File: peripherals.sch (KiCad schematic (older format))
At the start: 60 parts, among them J1 693022010811, J5 U_FL-R-SMT-1_10_, J6 U_FL-R-SMT-1_10_, J7 DM3AT-SF-PEJM5, U6 NCP163ASN330T1G

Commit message: Started placing main components on PCB. Change of RT battery model and USB flash connector
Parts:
- gave numbers to parts that had none: 21
- renumbered C47 to C100, C48 to C101, C49 to C102, C50 to C103, C51 to C104, C52 to C105, C53 to C106, C54 to C107, C34 to C87, C35 to C88, C36 to C89, C37 to C90, C38 to C91, C39 to C92, C40 to C93, C41 to C94, C42 to C95, C43 to C96, C44 to C97, C45 to C98, C46 to C99, D2 to D16, J1 to J8, L4 to L20, L5 to L21, R38 to R100, R40 to R101, R31 to R91, R32 to R92, R33 to R93, R34 to R94, R36 to R98, R37 to R99, U6 to U10

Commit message: Removed mounting pad for GNSS, changed main antenna model, added wifi ufl connector
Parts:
- removed ANT1: GPS-ANT050-external-antenna, sc606-baseboard-footprints:GPS-ANT050-mounting-pad, symbol sc606-baseboard:GPS-ANT050-external-antenna
- removed ANT2: PRO-OB-572_DCPOL, sc606-baseboard-footprints:PRO-OB-572_2, symbol sc606-baseboard:PRO-OB-572_DCPOL
- removed C102, C103, C89, C91: C_0p5_0402, sc606-baseboard-footprints:0402-cap, symbol sc606-baseboard:C_0p5_0402
- removed C92: C_6p9_0402, sc606-baseboard-footprints:0402-cap, symbol sc606-baseboard:C_6p9_0402
- removed C94: C_0p9_0402, sc606-baseboard-footprints:0402-cap, symbol sc606-baseboard:C_0p9_0402
- removed L20: LQW15AN2N4B00D, sc606-baseboard-footprints:0402-res, symbol sc606-baseboard:LQW15AN2N4B00D
- added C?: C_3p_0402, antmicro-footprints:0402-cap, symbol antmicroCapacitors0402:C_3p_0402
- added C? (x2): C_1u_0402, sc606-baseboard-footprints:0402-cap, symbol sc606-baseboard:C_1u_0402
- added E?: ANT-LTE-CER-T, sc606-baseboard-footprints:XDCR_ANT-LTE-CER-T, symbol sc606-baseboard:ANT-LTE-CER-T
- added J?: U_FL-R-SMT-1_10_, sc606-baseboard-footprints:Coax_Conn_U.FL, symbol sc606-baseboard:U_FL-R-SMT-1_10_
- added L?: HK10056N8S-T, antmicro-footprints:INDC1005X55N, symbol antmicroFixedInductors:HK10056N8S-T
- added R? (x4): R_0R_0402, antmicro-footprints:0402-res, symbol antmicroResistors0402:R_0R_0402
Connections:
- net labels added: ANT-WIFI
- wire segments 151 -> 155
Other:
- note added: "Wi-Fi Antenna\n"
- note removed: "Mounting Pad for GNSS Antenna\n"
- moved on the sheet: C101, C87, C88, C90, C93, C95, C96, C98, C99, J5, J6, L21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

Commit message: Added USB A and C double stack connector
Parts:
- C92: renamed from C?; footprint antmicro-footprints:0402-cap -> sc606-baseboard-footprints:0402-cap; symbol antmicroCapacitors0402:C_3p_0402 -> sc606-baseboard:C_3p_0402
- L20: renamed from L?; footprint antmicro-footprints:INDC1005X55N -> sc606-baseboard-footprints:INDC1005X55N; symbol antmicroFixedInductors:HK10056N8S-T -> sc606-baseboard:HK10056N8S-T
- R126, R127, R128, R129: renamed from R?; footprint antmicro-footprints:0402-res -> sc606-baseboard-footprints:0402-res; symbol antmicroResistors0402:R_0R_0402 -> sc606-baseboard:R_0R_0402
- gave numbers to parts that had none: 4
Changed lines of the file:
@@
 	8100 7750 8100 8050
 $Comp
-L sc606-baseboard:ANT-LTE-CER-T E?
+L sc606-baseboard:ANT-LTE-CER-T E1
 U 1 1 620E9422
 P 3450 7650
-F 0 "E?" H 3534 7679 50  0000 L CNN
+F 0 "E1" H 3534 7679 50  0000 L CNN
 F 1 "ANT-LTE-CER-T" H 3534 7588 50  0000 L CNN
 F 2 "sc606-baseboard-footprints:XDCR_ANT-LTE-CER-T" H 3450 7350 50  0001 L BNN
@@
 $EndComp
 $Comp
-L antmicroCapacitors0402:C_3p_0402 C?
+L sc606-baseboard:C_3p_0402 C92
 U 1 1 6212C05D
 P 2400 7650
-F 0 "C?" V 2142 7650 60  0000 C CNN
+F 0 "C92" V 2142 7650 60  0000 C CNN
 F 1 "C_3p_0402" H 2400 7500 60  0001 C CNN
-F 2 "antmicro-footprints:0402-cap" H 2600 7850 60  0001 L CNN
+F 2 "sc606-baseboard-footprints:0402-cap" H 2600 7850 60  0001 L CNN
 F 3 "" H 2400 7650 50  0001 C CNN
 F 4 "MULTICOMP" H 2600 8050 60  0001 L CNN "Manufacturer"
@@
 	2650 7650 2600 7650
 $Comp
-L sc606-baseboard:GND #PWR?
+L sc606-baseboard:GND #PWR0101
 U 1 1 62165D99
 P 2600 8600
-F 0 "#PWR?" H 2600 8350 50  0001 C CNN
+F 0 "#PWR0101" H 2600 8350 50  0001 C CNN
 F 1 "GND" H 2605 8427 50  0000 C CNN
 F 2 "" H 2600 8600 50  0001 C CNN
@@
 $EndComp
 $Comp
-L sc606-baseboard:GND #PWR?
+L sc606-baseboard:GND #PWR0157
 U 1 1 6216613F
 P 3050 7950
-F 0 "#PWR?" H 3050 7700 50  0001 C CNN
+F 0 "#PWR0157" H 3050 7700 50  0001 C CNN
 F 1 "GND" H 3055 7777 50  0000 C CNN
 F 2 "" H 3050 7950 50  0001 C CNN
@@
 $EndComp
 $Comp
-L sc606-baseboard:GND #PWR?
+L sc606-baseboard:GND #PWR0158
 U 1 1 62166933
 P 2150 7950
-F 0 "#PWR?" H 2150 7700 50  0001 C CNN
+F 0 "#PWR0158" H 2150 7700 50  0001 C CNN
 F 1 "GND" H 2155 7777 50  0000 C CNN
 F 2 "" H 2150 7950 50  0001 C CNN
@@
 $EndComp
 $Comp
-L sc606-baseboard:GND #PWR?
+L sc606-baseboard:GND #PWR0159
 U 1 1 62166E12
 P 3350 7950
-F 0 "#PWR?" H 3350 7700 50  0001 C CNN
+F 0 "#PWR0159" H 3350 7700 50  0001 C CNN
 F 1 "GND" H 3355 7777 50  0000 C CNN
 F 2 "" H 3350 7950 50  0001 C CNN
@@
 	3350 7750 3350 7950
 $Comp
-L antmicroResistors0402:R_0R_0402 R?
+L sc606-baseboard:R_0R_0402 R128
 U 1 1 621B97C1
 P 2800 7650
-F 0 "R?" H 2800 7863 60  0000 C CNN
+F 0 "R128" H 2800 7863 60  0000 C CNN
 F 1 "R_0R_0402" H 2800 7500 60  0001 C CNN
-F 2 "antmicro-footprints:0402-res" H 3000 7850 60  0001 L CNN
+F 2 "sc606-baseboard-footprints:0402-res" H 3000 7850 60  0001 L CNN
 F 3 "" H 2800 7650 50  0001 C CNN
 F 4 "PANASONIC" H 3000 8050 60  0001 L CNN "Manufacturer"
@@
 $EndComp
 $Comp
-L antmicroResistors0402:R_0R_0402 R?
+L sc606-baseboard:R_0R_0402 R127
 U 1 1 621B9CE0
 P 2150 7800
-F 0 "R?" V 2059 7870 60  0000 L CNN
+F 0 "R127" V 2059 7870 60  0000 L CNN
 F 1 "R_0R_0402" H 2150 7650 60  0001 C CNN
-F 2 "antmicro-footprints:0402-res" H 2350 8000 60  0001 L CNN
+F 2 "sc606-baseboard-footprints:0402-res" H 2350 8000 60  0001 L CNN
 F 3 "" H 2150 7800 50  0001 C CNN
 F 4 "PANASONIC" H 2350 8200 60  0001 L CNN "Manufacturer"
@@
 	2950 7650 3050 7650
 $Comp
-L antmicroResistors0402:R_0R_0402 R?
+L sc606-baseboard:R_0R_0402 R129
 U 1 1 621BD57F
 P 3050 7800
-F 0 "R?" V 2959 7870 60  0000 L CNN
+F 0 "R129" V 2959 7870 60  0000 L CNN
 F 1 "R_0R_0402" H 3050 7650 60  0001 C CNN
-F 2 "antmicro-footprints:0402-res" H 3250 8000 60  0001 L CNN
+F 2 "sc606-baseboard-footprints:0402-res" H 3250 8000 60  0001 L CNN
 F 3 "" H 3050 7800 50  0001 C CNN
 F 4 "PANASONIC" H 3250 8200 60  0001 L CNN "Manufacturer"
@@
 	3050 7650 3350 7650
 $Comp
-L antmicroFixedInductors:HK10056N8S-T L?
+L sc606-baseboard:HK10056N8S-T L20
 U 1 1 621F9A28
 P 2600 8300
-F 0 "L?" V 2554 8344 50  0000 L CNN
+F 0 "L20" V 2554 8344 50  0000 L CNN
 F 1 "HK10056N8S-T" V 2645 8344 50  0000 L CNN
-F 2 "antmicro-footprints:INDC1005X55N" H 2600 8200 50  0001 C BNN
+F 2 "sc606-baseboard-footprints:INDC1005X55N" H 2600 8200 50  0001 C BNN
 F 3 "https://www.mouser.pl/datasheet/2/396/mlci04_e-1396612.pdf" H 2600 8300 50  0001 L BNN
 F 4 "Taiyo Yuden" H 2600 8150 50  0001 C CNN "Manufacturer"
@@
 Wi-Fi Antenna\n
 $Comp
-L sc606-baseboard:U_FL-R-SMT-1_10_ J?
+L sc606-baseboard:U_FL-R-SMT-1_10_ J12
 U 1 1 6221D1B4
 P 2900 9600
-F 0 "J?" H 2812 9613 50  0000 R CNN
+F 0 "J12" H 2812 9613 50  0000 R CNN
 F 1 "U_FL-R-SMT-1_10_" H 2812 9522 50  0000 R CNN
 F 2 "sc606-baseboard-footprints:Coax_Conn_U.FL" H 3100 9800 60  0001 L CNN
@@
 ANT-WIFI
 $Comp
-L antmicroResistors0402:R_0R_0402 R?
+L sc606-baseboard:R_0R_0402 R126
 U 1 1 62231121
 P 2100 9600
-F 0 "R?" H 2100 9813 60  0000 C CNN
+F 0 "R126" H 2100 9813 60  0000 C CNN
 F 1 "R_0R_0402" H 2100 9450 60  0001 C CNN
-F 2 "antmicro-footprints:0402-res" H 2300 9800 60  0001 L CNN
+F 2 "sc606-baseboard-footprints:0402-res" H 2300 9800 60  0001 L CNN
 F 3 "" H 2100 9600 50  0001 C CNN
 F 4 "PANASONIC" H 2300 10000 60  0001 L CNN "Manufacturer"
@@
 $EndComp
 $Comp
-L sc606-baseboard:C_1u_0402 C?
+L sc606-baseboard:C_1u_0402 C89
 U 1 1 62233FFC
 P 1850 9950
-F 0 "C?" H 1900 10050 60  0000 L CNN
+F 0 "C89" H 1900 10050 60  0000 L CNN
 F 1 "C_1u_0402" H 1850 9800 60  0001 C CNN
 F 2 "sc606-baseboard-footprints:0402-cap" H 2050 10150 60  0001 L CNN
@@
 $EndComp
 $Comp
-L sc606-baseboard:C_1u_0402 C?
+L sc606-baseboard:C_1u_0402 C91
 U 1 1 62236B43
 P 2350 9950
-F 0 "C?" H 2400 10050 60  0000 L CNN
+F 0 "C91" H 2400 10050 60  0000 L CNN
 F 1 "C_1u_0402" H 2350 9800 60  0001 C CNN
 F 2 "sc606-baseboard-footprints:0402-cap" H 2550 10150 60  0001 L CNN
@@
 $EndComp
 $Comp
-L sc606-baseboard:GND #PWR?
+L sc606-baseboard:GND #PWR0160
 U 1 1 6223716E
 P 1850 10250
-F 0 "#PWR?" H 1850 10000 50  0001 C CNN
+F 0 "#PWR0160" H 1850 10000 50  0001 C CNN
 F 1 "GND" H 1855 10077 50  0000 C CNN
 F 2 "" H 1850 10250 50  0001 C CNN
@@
 $EndComp
 $Comp
-L sc606-baseboard:GND #PWR?
+L sc606-baseboard:GND #PWR0161
 U 1 1 6223764D
 P 2350 10250
-F 0 "#PWR?" H 2350 10000 50  0001 C CNN
+F 0 "#PWR0161" H 2350 10000 50  0001 C CNN
 F 1 "GND" H 2355 10077 50  0000 C CNN
 F 2 "" H 2350 10250 50  0001 C CNN
@@
 $EndComp
 $Comp
-L sc606-baseboard:GND #PWR?
+L sc606-baseboard:GND #PWR0162
 U 1 1 622379B0
 P 2900 9850
-F 0 "#PWR?" H 2900 9600 50  0001 C CNN
+F 0 "#PWR0162" H 2900 9600 50  0001 C CNN
 F 1 "GND" H 2905 9677 50  0000 C CNN
 F 2 "" H 2900 9850 50  0001 C CNN

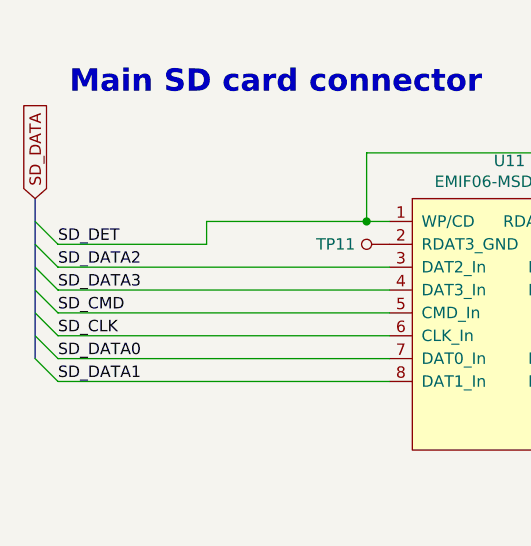
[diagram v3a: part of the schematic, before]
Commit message: Main components placed on board
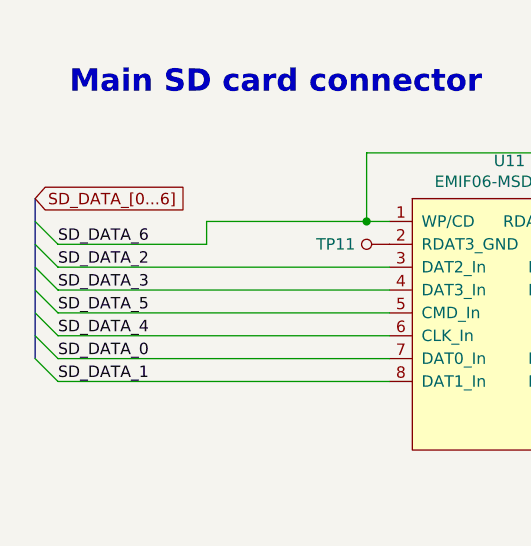
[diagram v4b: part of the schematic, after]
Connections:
- net SD_CLK renamed SD_DATA_4
- net SD_CMD renamed SD_DATA_5
- net SD_DATA0 renamed SD_DATA_0
- net SD_DATA1 renamed SD_DATA_1
- net SD_DATA2 renamed SD_DATA_2
- net SD_DATA3 renamed SD_DATA_3
- net SD_DET renamed SD_DATA_6
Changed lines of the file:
@@
 Main SD card connector
 Text Label 800  1650 0    50   ~ 0
-SD_DET
+SD_DATA_6
 Text Label 800  1850 0    50   ~ 0
-SD_DATA3
+SD_DATA_3
 Text Label 800  1750 0    50   ~ 0
-SD_DATA2
+SD_DATA_2
 Text Label 800  2250 0    50   ~ 0
-SD_DATA1
+SD_DATA_1
 Text Label 800  2150 0    50   ~ 0
-SD_DATA0
+SD_DATA_0
 Text Label 800  1950 0    50   ~ 0
-SD_CMD
+SD_DATA_5
 Text Label 800  2050 0    50   ~ 0
-SD_CLK
+SD_DATA_4
 Wire Wire Line
 	800  1650 1450 1650
@@
 Entry Wire Line
 	700  2150 800  2250
-Text GLabel 700  1450 1    50   Input ~ 0
-SD_DATA
+Text GLabel 700  1450 2    50   Input ~ 0
+SD_DATA_[0...6]
 Text GLabel 3850 1200 1    50   Input ~ 0
 SD_LDO11

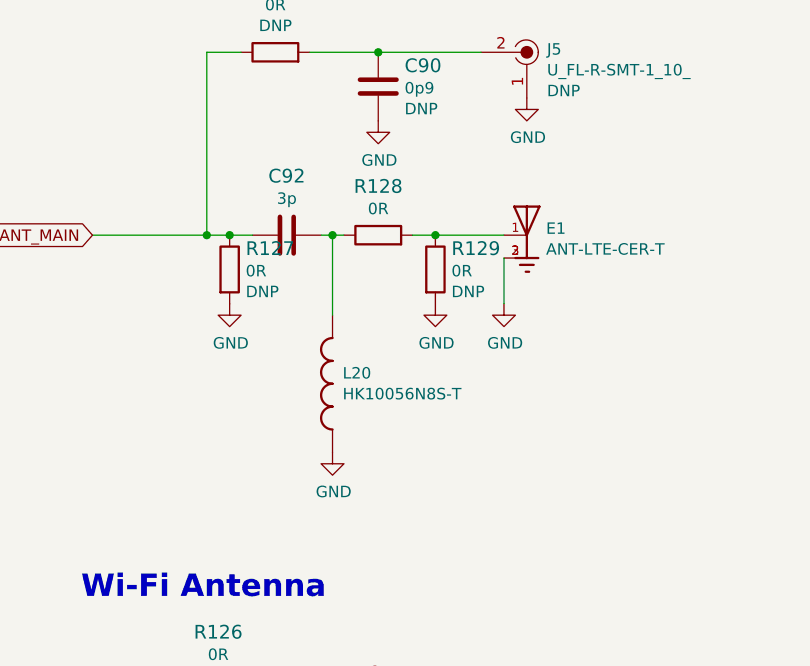
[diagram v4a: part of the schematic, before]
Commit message: FFC and general display camera connectors distributed on board
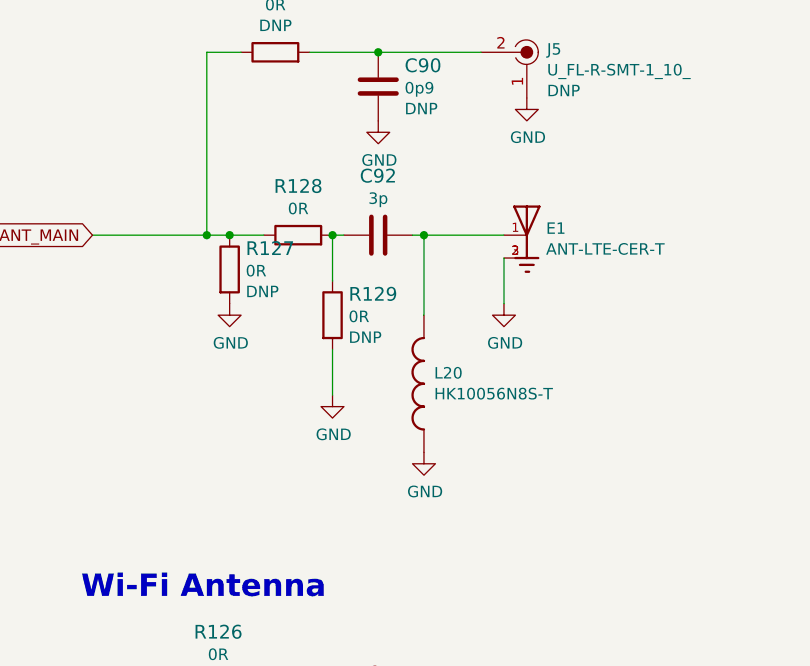
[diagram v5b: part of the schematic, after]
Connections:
- net ANT_MAIN: now also R128.1; no longer C92.2
- net at R128.2, R129.1: now also C92.2; no longer E1.1
- net at C92.1, L20.1: now also E1.1; no longer R128.1
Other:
- moved on the sheet: C92, L20, R128, R129
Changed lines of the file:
@@
 L sc606-baseboard:C_3p_0402 C92
 U 1 1 6212C05D
-P 2400 7650
-F 0 "C92" V 2142 7650 60  0000 C CNN
-F 1 "C_3p_0402" H 2400 7500 60  0001 C CNN
-F 2 "sc606-baseboard-footprints:0402-cap" H 2600 7850 60  0001 L CNN
-F 3 "" H 2400 7650 50  0001 C CNN
-F 4 "MULTICOMP" H 2600 8050 60  0001 L CNN "Manufacturer"
-F 5 "MC0402N3R0C500CT" H 2600 7950 60  0001 L CNN "MPN"
-F 6 "3p" V 2240 7650 50  0000 C CNN "Val"
-	1    2400 7650
-	0    1    1    0
-$EndComp
-Wire Wire Line
-	2250 7650 2150 7650
+P 2800 7650
+F 0 "C92" V 2542 7650 60  0000 C CNN
+F 1 "C_3p_0402" H 2800 7500 60  0001 C CNN
+F 2 "sc606-baseboard-footprints:0402-cap" H 3000 7850 60  0001 L CNN
+F 3 "" H 2800 7650 50  0001 C CNN
+F 4 "MULTICOMP" H 3000 8050 60  0001 L CNN "Manufacturer"
+F 5 "MC0402N3R0C500CT" H 3000 7950 60  0001 L CNN "MPN"
+F 6 "3p" V 2640 7650 50  0000 C CNN "Val"
+	1    2800 7650
+	0    1    1    0
+$EndComp
+Wire Wire Line
+	2300 7650 2150 7650
 Connection ~ 2050 7650
 Wire Wire Line
@@
 L sc606-baseboard:GND #PWR0101
 U 1 1 62165D99
-P 2600 8600
-F 0 "#PWR0101" H 2600 8350 50  0001 C CNN
-F 1 "GND" H 2605 8427 50  0000 C CNN
-F 2 "" H 2600 8600 50  0001 C CNN
-F 3 "" H 2600 8600 50  0001 C CNN
-	1    2600 8600
+P 3000 8600
+F 0 "#PWR0101" H 3000 8350 50  0001 C CNN
+F 1 "GND" H 3005 8427 50  0000 C CNN
+F 2 "" H 3000 8600 50  0001 C CNN
+F 3 "" H 3000 8600 50  0001 C CNN
+	1    3000 8600
 	1    0    0    -1
 $EndComp
@@
 L sc606-baseboard:GND #PWR0157
 U 1 1 6216613F
-P 3050 7950
-F 0 "#PWR0157" H 3050 7700 50  0001 C CNN
-F 1 "GND" H 3055 7777 50  0000 C CNN
-F 2 "" H 3050 7950 50  0001 C CNN
-F 3 "" H 3050 7950 50  0001 C CNN
-	1    3050 7950
+P 2600 8350
+F 0 "#PWR0157" H 2600 8100 50  0001 C CNN
+F 1 "GND" H 2605 8177 50  0000 C CNN
+F 2 "" H 2600 8350 50  0001 C CNN
+F 3 "" H 2600 8350 50  0001 C CNN
+	1    2600 8350
 	1    0    0    -1
 $EndComp
@@
 L sc606-baseboard:R_0R_0402 R128
 U 1 1 621B97C1
-P 2800 7650
-F 0 "R128" H 2800 7863 60  0000 C CNN
-F 1 "R_0R_0402" H 2800 7500 60  0001 C CNN
-F 2 "sc606-baseboard-footprints:0402-res" H 3000 7850 60  0001 L CNN
-F 3 "" H 2800 7650 50  0001 C CNN
-F 4 "PANASONIC" H 3000 8050 60  0001 L CNN "Manufacturer"
-F 5 "ERJ2GE0R00X" H 3000 7950 60  0001 L CNN "MPN"
-F 6 "0R" H 2800 7765 50  0000 C CNN "Val"
-	1    2800 7650
+P 2450 7650
+F 0 "R128" H 2450 7863 60  0000 C CNN
+F 1 "R_0R_0402" H 2450 7500 60  0001 C CNN
+F 2 "sc606-baseboard-footprints:0402-res" H 2650 7850 60  0001 L CNN
+F 3 "" H 2450 7650 50  0001 C CNN
+F 4 "PANASONIC" H 2650 8050 60  0001 L CNN "Manufacturer"
+F 5 "ERJ2GE0R00X" H 2650 7950 60  0001 L CNN "MPN"
+F 6 "0R" H 2450 7765 50  0000 C CNN "Val"
+	1    2450 7650
 	1    0    0    -1
 $EndComp
@@
 Wire Wire Line
 	2150 7650 2050 7650
-Wire Wire Line
-	2950 7650 3050 7650
 $Comp
 L sc606-baseboard:R_0R_0402 R129
 U 1 1 621BD57F
-P 3050 7800
-F 0 "R129" V 2959 7870 60  0000 L CNN
-F 1 "R_0R_0402" H 3050 7650 60  0001 C CNN
-F 2 "sc606-baseboard-footprints:0402-res" H 3250 8000 60  0001 L CNN
-F 3 "" H 3050 7800 50  0001 C CNN
-F 4 "PANASONIC" H 3250 8200 60  0001 L CNN "Manufacturer"
-F 5 "ERJ2GE0R00X" H 3250 8100 60  0001 L CNN "MPN"
-F 6 "0R" V 3057 7870 50  0000 L CNN "Val"
-F 7 "DNP" V 3148 7870 50  0000 L CNN "DNP"
-	1    3050 7800
-	0    1    1    0
-$EndComp
-Connection ~ 3050 7650
-Wire Wire Line
-	3050 7650 3350 7650
+P 2600 8000
+F 0 "R129" V 2509 8070 60  0000 L CNN
+F 1 "R_0R_0402" H 2600 7850 60  0001 C CNN
+F 2 "sc606-baseboard-footprints:0402-res" H 2800 8200 60  0001 L CNN
+F 3 "" H 2600 8000 50  0001 C CNN
+F 4 "PANASONIC" H 2800 8400 60  0001 L CNN "Manufacturer"
+F 5 "ERJ2GE0R00X" H 2800 8300 60  0001 L CNN "MPN"
+F 6 "0R" V 2607 8070 50  0000 L CNN "Val"
+F 7 "DNP" V 2698 8070 50  0000 L CNN "DNP"
+	1    2600 8000
+	0    1    1    0
+$EndComp
 $Comp
 L sc606-baseboard:HK10056N8S-T L20
 U 1 1 621F9A28
-P 2600 8300
-F 0 "L20" V 2554 8344 50  0000 L CNN
-F 1 "HK10056N8S-T" V 2645 8344 50  0000 L CNN
-F 2 "sc606-baseboard-footprints:INDC1005X55N" H 2600 8200 50  0001 C BNN
-F 3 "https://www.mouser.pl/datasheet/2/396/mlci04_e-1396612.pdf" H 2600 8300 50  0001 L BNN
-F 4 "Taiyo Yuden" H 2600 8150 50  0001 C CNN "Manufacturer"
-F 5 "HK10056N8S-T" H 2600 8050 50  0001 C CNN "MPN"
-	1    2600 8300
-	0    1    1    0
-$EndComp
-Wire Wire Line
-	2600 8000 2600 7650
-Connection ~ 2600 7650
-Wire Wire Line
-	2600 7650 2550 7650
+P 3000 8300
+F 0 "L20" V 2954 8344 50  0000 L CNN
+F 1 "HK10056N8S-T" V 3045 8344 50  0000 L CNN
+F 2 "sc606-baseboard-footprints:INDC1005X55N" H 3000 8200 50  0001 C BNN
+F 3 "https://www.mouser.pl/datasheet/2/396/mlci04_e-1396612.pdf" H 3000 8300 50  0001 L BNN
+F 4 "Taiyo Yuden" H 3000 8150 50  0001 C CNN "Manufacturer"
+F 5 "HK10056N8S-T" H 3000 8050 50  0001 C CNN "MPN"
+	1    3000 8300
+	0    1    1    0
+$EndComp
+Wire Wire Line
+	3000 8000 3000 7650
+Wire Wire Line
+	3000 7650 2950 7650
 Text Notes 1500 9250 0    98   ~ 20
 Wi-Fi Antenna\n
@@
 Wire Wire Line
 	2350 10100 2350 10250
+Wire Wire Line
+	3350 7650 3000 7650
+Connection ~ 3000 7650
+Wire Wire Line
+	2600 7850 2600 7650
+Connection ~ 2600 7650
+Wire Wire Line
+	2600 8350 2600 8150
 Wire Bus Line
 	700  1450 700  2150
